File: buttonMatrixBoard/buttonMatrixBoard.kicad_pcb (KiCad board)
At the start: 2 copper layers, 80 x 40 mm, 42 parts, among them J1 Conn_01x04_Pin, J2 Conn_01x02_Pin, J3 Conn_01x02_Pin, J4 Conn_01x04_Pin, J5 Conn_01x04_Pin, J6 Conn_01x03_Pin, SW1 SW_Push, SW2 SW_Push, SW3 SW_Push, SW4 SW_Push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

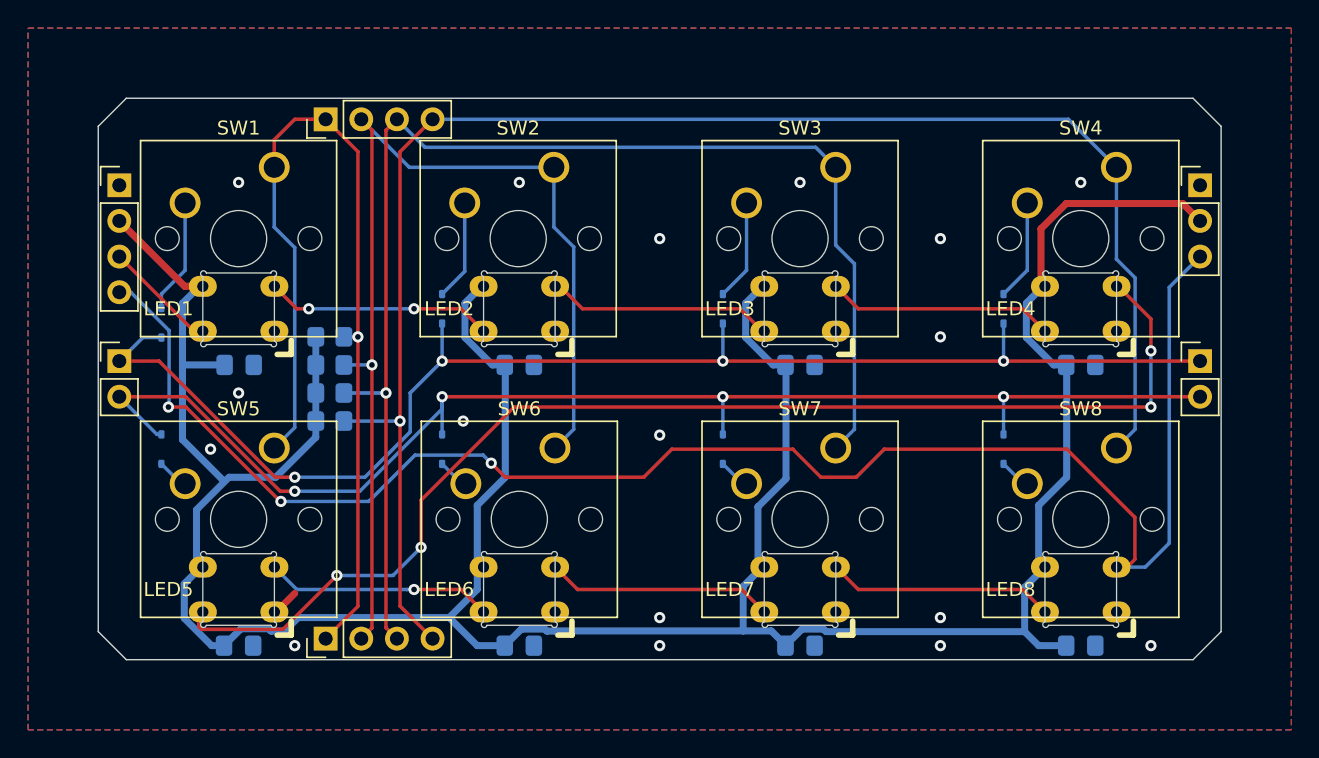
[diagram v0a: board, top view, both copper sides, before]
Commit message: fixed footprint problems on first order
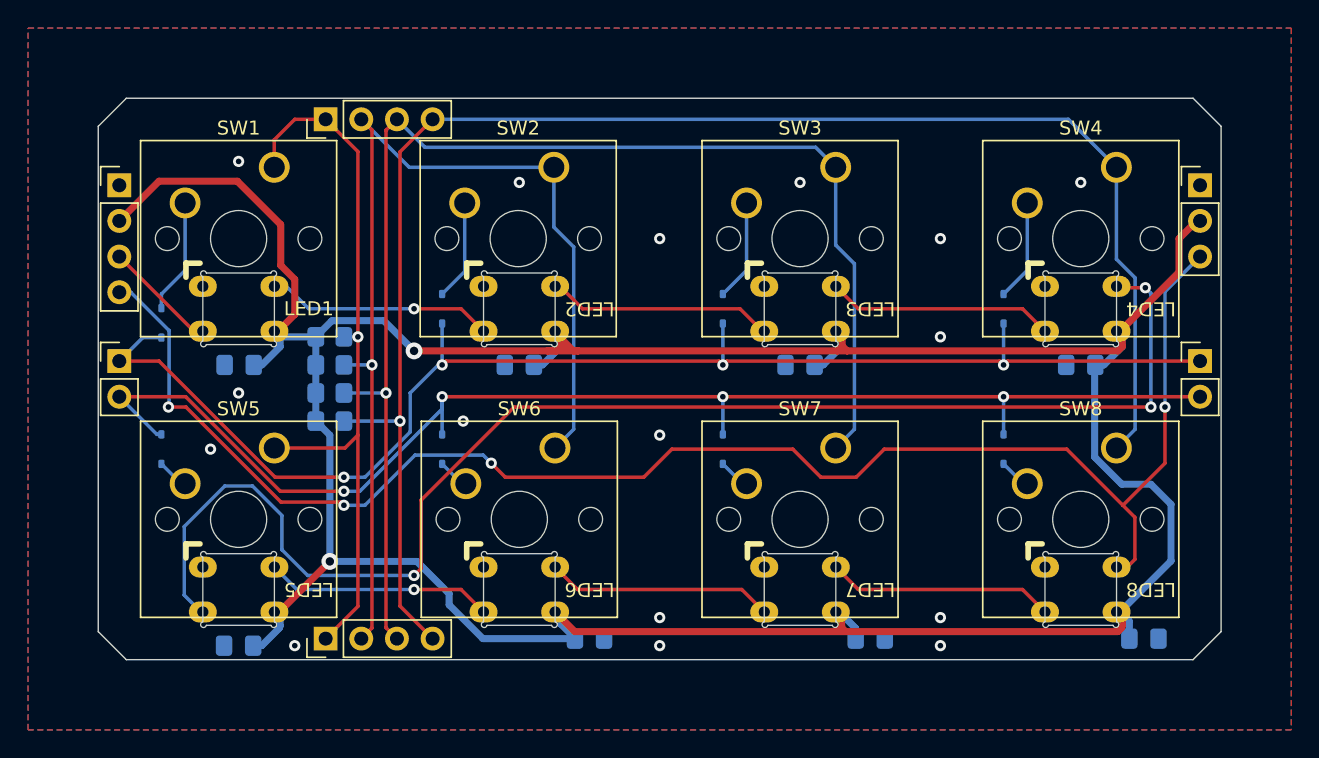
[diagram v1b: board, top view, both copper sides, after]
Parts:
- moved C6 5.02 mm to (35.0, 38.5)
- moved C7 5.02 mm to (55.0, 38.5)
- moved C8 4.53 mm to (74.5, 38.5)
- turned C1 to 0 degrees
- turned C2 to 0 degrees
- turned C3 to 0 degrees
- turned C4 to 0 degrees
- turned C5 to 0 degrees
- turned LED1 to 180 degrees
- turned LED2 to 180 degrees
- turned LED3 to 180 degrees
- turned LED4 to 180 degrees
- turned LED5 to 180 degrees
- turned LED6 to 180 degrees
- turned LED7 to 180 degrees
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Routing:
- net Sense1: track 67.3 -> 52.5 mm
- net VCC: track 220.1 -> 234.2 mm, vias 0 -> 2
- net Net-(LED4-DOUT): track 87.1 -> 99.4 mm, vias 4 -> 3
- net Led Out: track 118.4 -> 112.9 mm, vias 3 -> 4
- net GND: track 2.10 -> 0.75 mm, vias 17 -> 16
- net Pull1: track 97.2 -> 98.5 mm
- net Net-(LED1-DOUT): track 16.1 -> 16.2 mm, vias 2 -> 1

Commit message: buttonMatrix changed Diode footprint
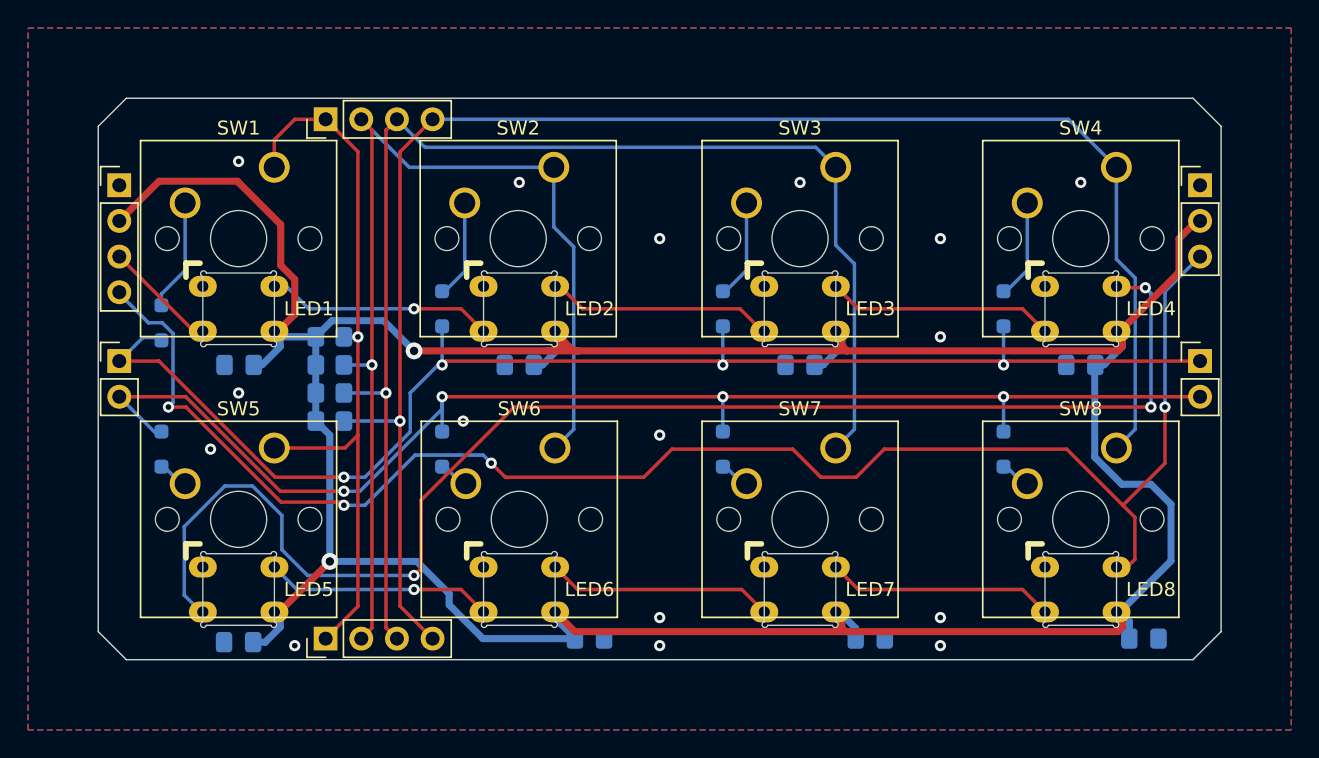
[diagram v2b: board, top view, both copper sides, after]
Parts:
- D1, D2, D3, D4, D5, D6, D7, D8: footprint Diode_SMD:D_SOD-323 -> Diode_SMD:D_SOD-323_HandSoldering
- moved C5 0.25 mm to (10.0, 38.8)
